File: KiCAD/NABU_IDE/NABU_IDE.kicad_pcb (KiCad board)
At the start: 2 copper layers, 108.5 x 71.1 mm, 36 parts, among them J1 IDE ATA Bus, J2 NABU Expansion Header, J3 NABU Daisy Chain In, J4 NABU Daisy Chain Out, J5 NABU External Power, U1 74LS245, U2 74LS32, U3 74LS08, U4 74LS04, U5 74LS32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

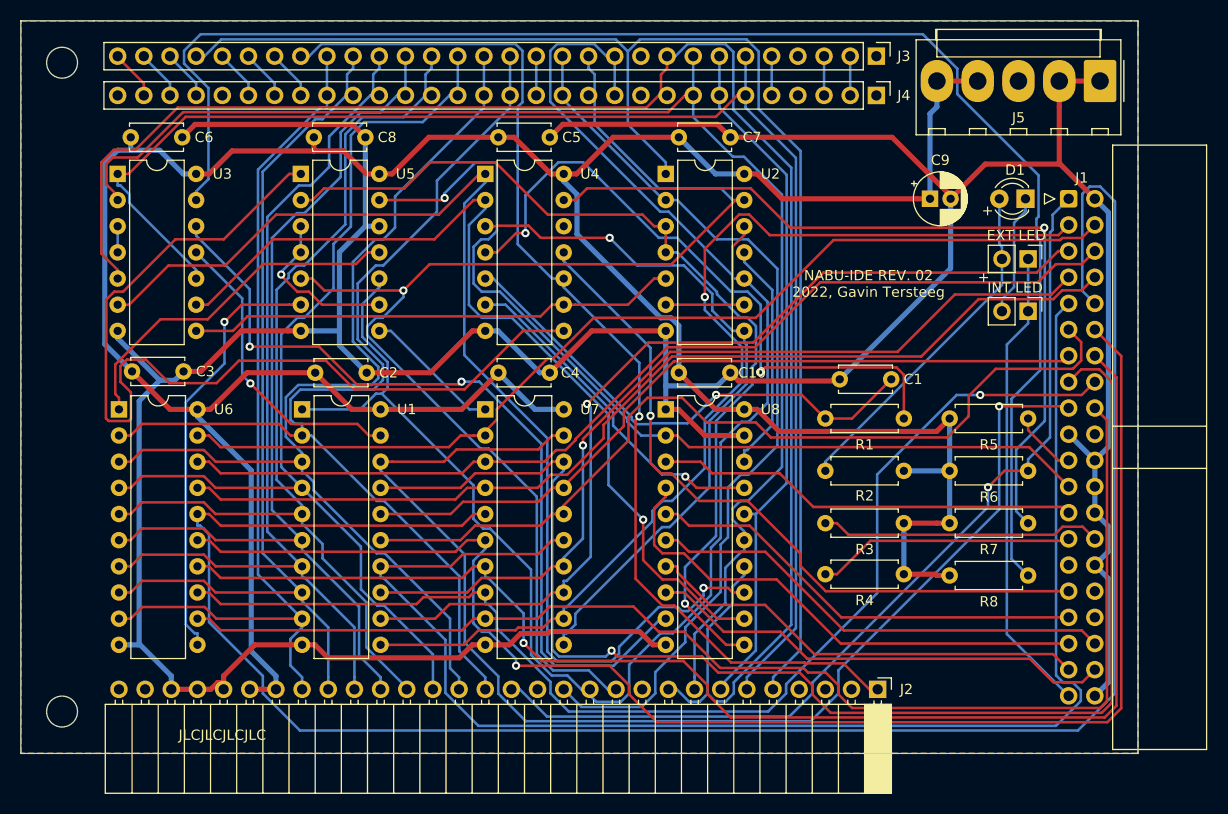
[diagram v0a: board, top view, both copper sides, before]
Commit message: Fixed power connector issue and added CF power option
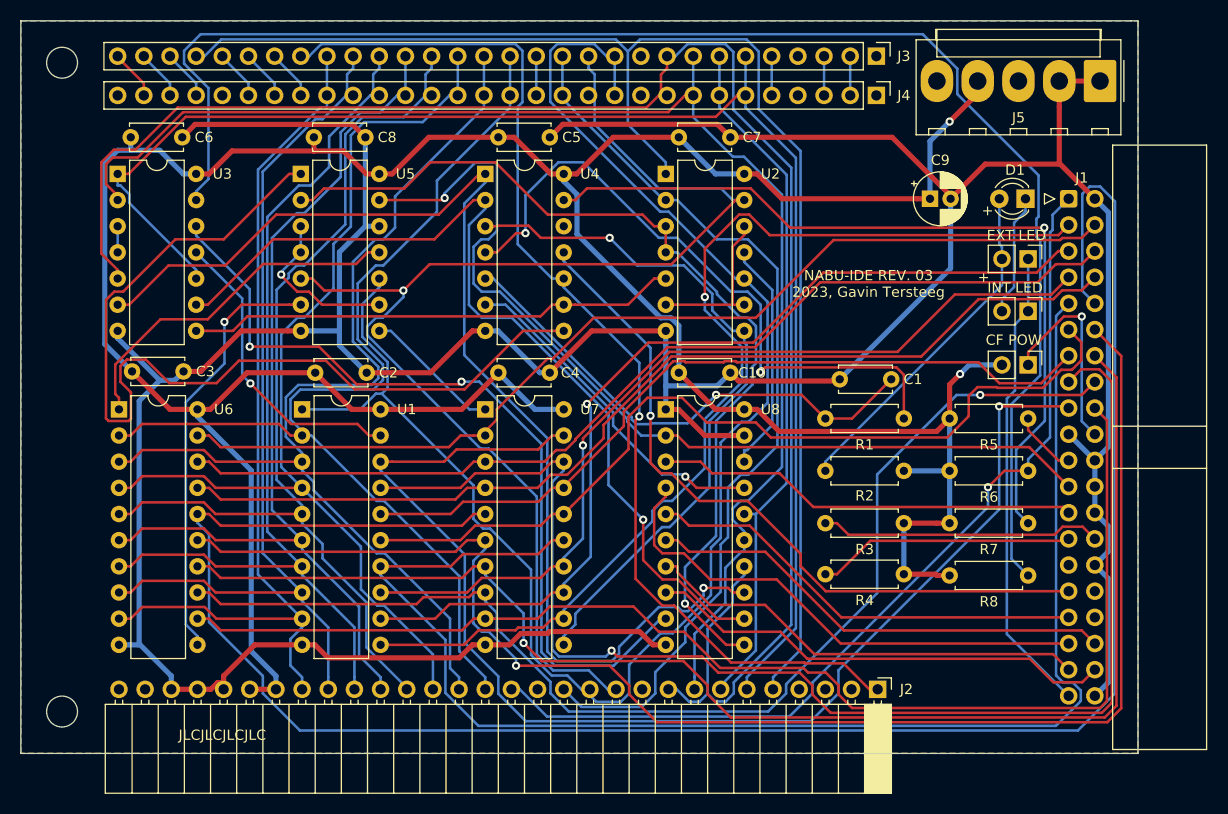
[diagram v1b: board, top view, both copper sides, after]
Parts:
- added JP3: CF Power Option, Connector_PinHeader_2.54mm:PinHeader_1x02_P2.54mm_Vertical, F.Cu at (157.6, 90.2)
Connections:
- J1 pad 20: (no net) -> /IDE_CFPOWER
- J5 pad 5: /+5V -> (no net)
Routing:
- net /IDE_CFPOWER: track 0.00 -> 19.8 mm, vias 0 -> 1
- net /+5V: track 294.3 -> 301.1 mm, vias 0 -> 2
- net /BUF_D2: track 74.2 -> 76.1 mm
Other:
- board text added: "CF POW"
- board text added: "NABU-IDE REV. 03 2023, Gavin Tersteeg"
- board text removed: "NABU-IDE REV. 02 2022, Gavin Tersteeg"
